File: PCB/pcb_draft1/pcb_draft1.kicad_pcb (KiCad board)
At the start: 2 copper layers, 100 x 100 mm, 83 parts, among them J1 RollerServos, J2 12V_Power A97996-ND, J3 HomeSwitch, J4 Therm1, J5 ArdAnalogTherm, J6 Therm2, J7 Conn_02x02_Odd_Even, Q1 DMN6140L, Q10 DMN6140L, Q11 DMN6140L, Q12 DMN6140L, Q13 DMN6140L, Q14 DMN6140L, Q15 DMN6140L, Q2 DMN6140L, Q3 DMN6140L, Q4 DMN6140L, Q5 DMN6140L, Q6 DMN6140L, Q7 DMN6140L, Q8 DMN6140L, Q9 DMN6140L, U1 STSPIN820, U2 STSPIN820, U3 AMS1117-5.0 RasPi, U4 AMS1117-5.0 Servo, Y1 Arduino_Mega_Bottom_Pins1

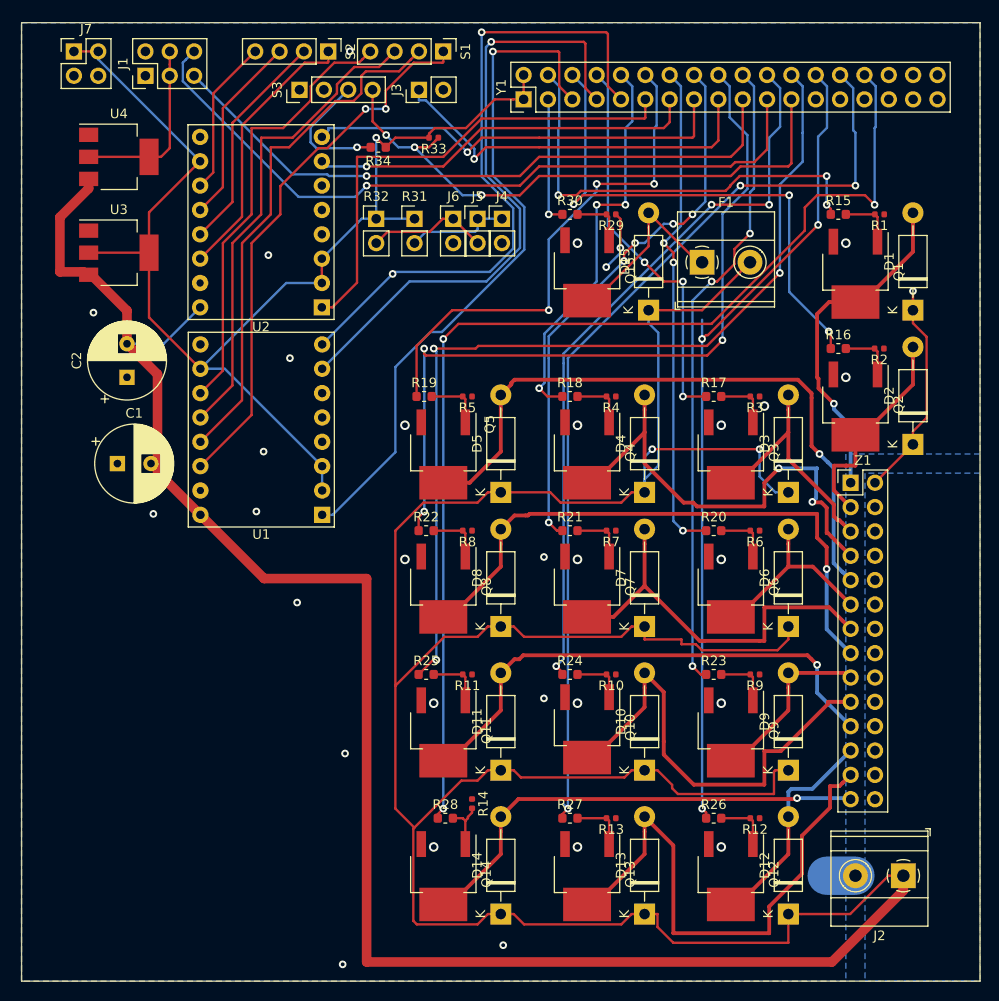
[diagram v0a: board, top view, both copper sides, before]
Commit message: Fix silkscreen and add holes
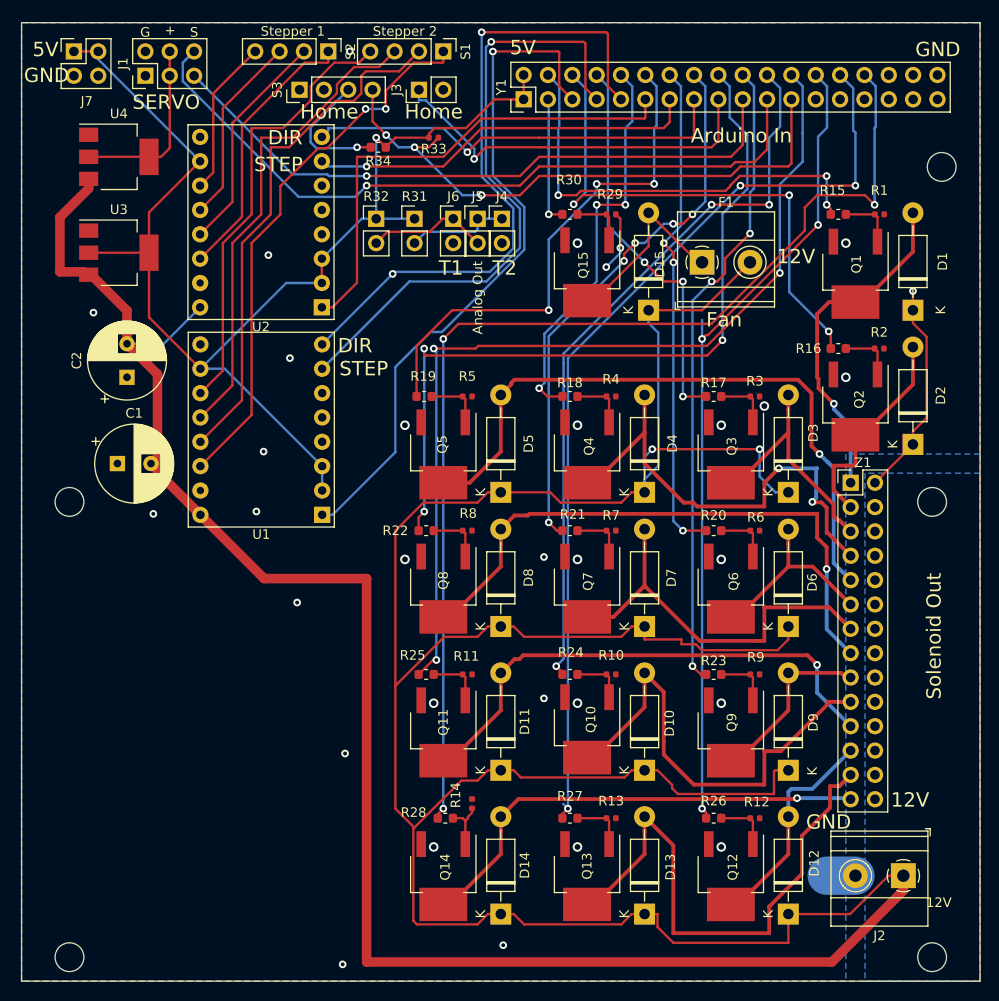
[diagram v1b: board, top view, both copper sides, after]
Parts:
- added 12V: MountingHole_3mm, MountingHole:MountingHole_3mm, F.Cu at (120.0, 112.5)
- added ?: MountingHole_3mm, MountingHole:MountingHole_3mm, F.Cu at (30.0, 112.5)
- added REF**: MountingHole_3mm, MountingHole:MountingHole_3mm, F.Cu at (120.0, 65.0)
- added REF**: MountingHole_3mm, MountingHole:MountingHole_3mm, F.Cu at (30.0, 65.0)
- added REF**: MountingHole_3mm, MountingHole:MountingHole_3mm, F.Cu at (121.0, 30.1)
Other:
- board text added: "+"
- board text added: "12V"
- board text added: "5V"
- board text added: "Analog Out"
- board text added: "Arduino In"
- board text added: "DIR"
- board text added: "Fan"
- board text added: "G"
- board text added: "GND"
- board text added: "Home"
- board text added: "S"
- board text added: "SERVO"
- board text added: "STEP"
- board text added: "Solenoid Out"
- board text added: "Stepper 1"
- board text added: "Stepper 2"
- board text added: "T1"
- board text added: "T2"

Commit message: Fix silkscreen and add holes
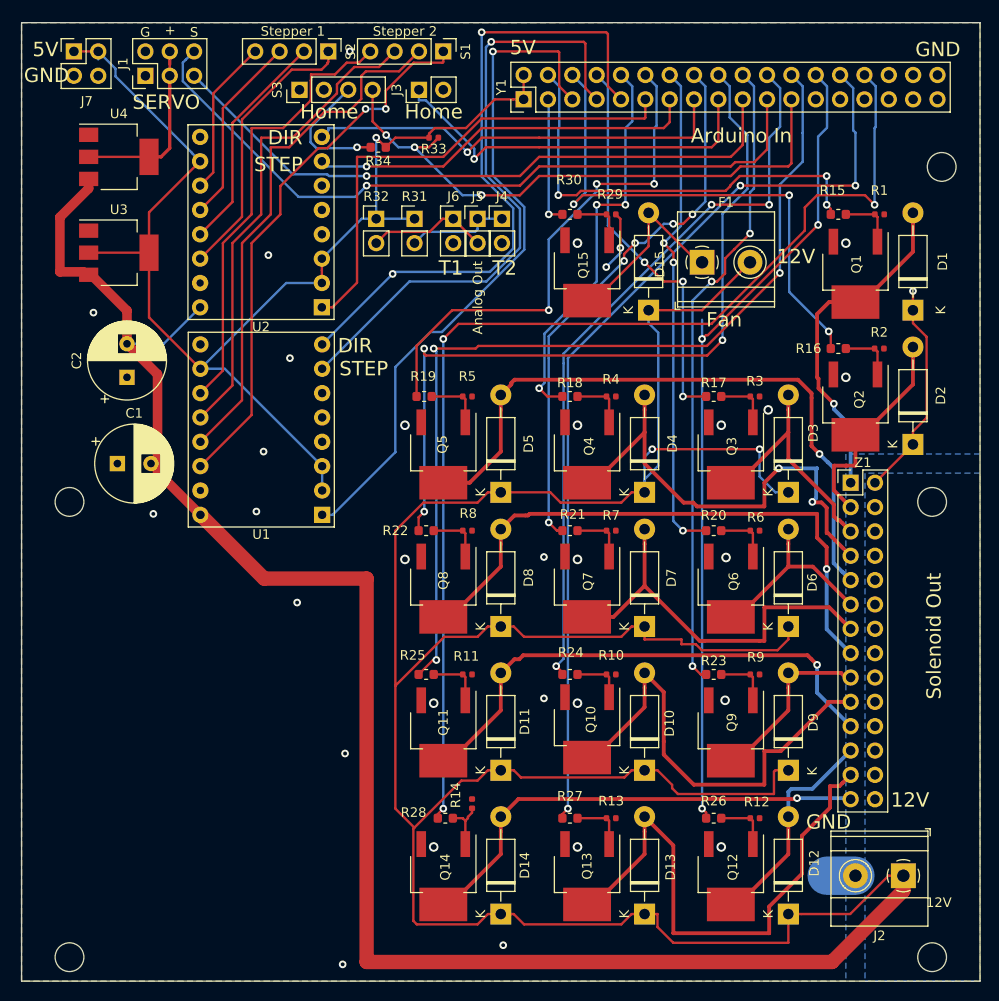
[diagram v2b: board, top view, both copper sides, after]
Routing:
- net 5V: track 129.7 -> 130.5 mm
- net Net-(S1-Pad4): track 46.4 -> 47.1 mm
- net Net-(R27-Pad1): track 98.6 -> 97.9 mm

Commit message: Pushing any new board stuff
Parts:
- added C3: C_0201_0603Metric, Capacitor_SMD:C_0201_0603Metric, F.Cu at (29.8, 44.2)
- added C4: C_0201_0603Metric, Capacitor_SMD:C_0201_0603Metric, F.Cu at (28.6, 31.3)
- added G***: LOGO, custom_symbols:dotdotdot, F.Cu at (42.4, 90.6)
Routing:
- net (no net): track 0.00 -> 5.08 mm, vias 0 -> 2
- net 12V: track 476.8 -> 480.3 mm
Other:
- board text added: "Megan Ku, Colin Snow, Nathan Weil, Annie Tor, and Maia Materman"
